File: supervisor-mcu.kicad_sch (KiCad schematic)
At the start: 20 parts, among them J21 ERF5-020-05.0-X-DV, J22 ERF5-020-05.0-X-DV

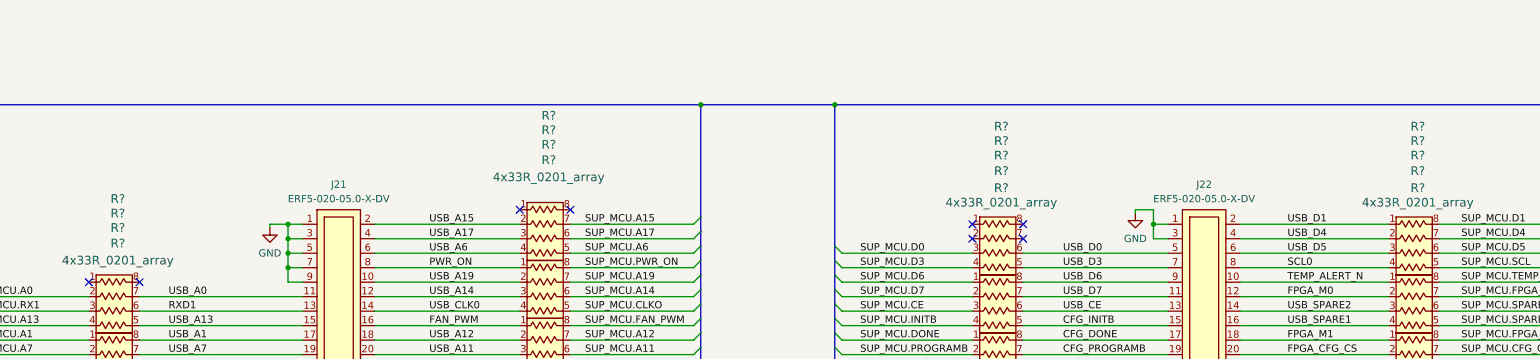
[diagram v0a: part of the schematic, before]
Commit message: Fix DDR3L placement
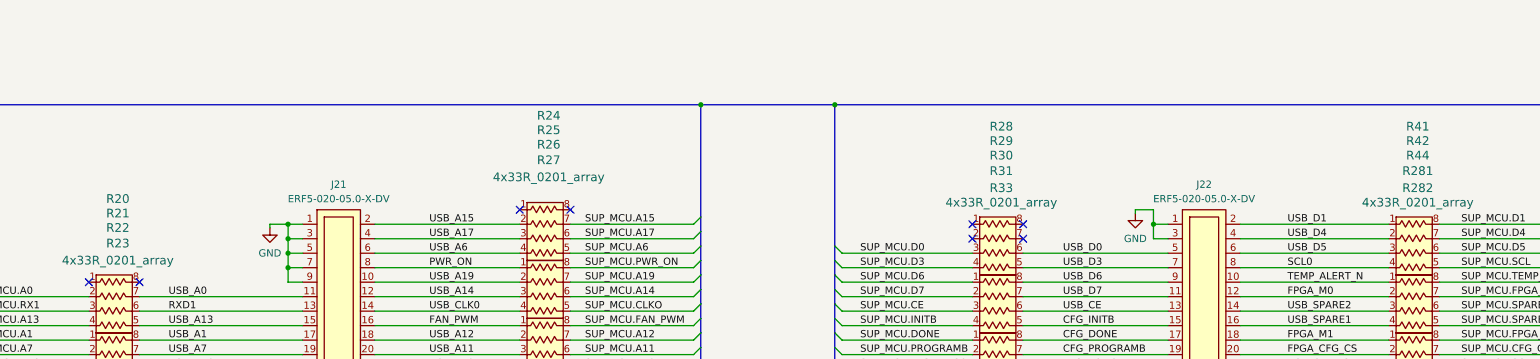
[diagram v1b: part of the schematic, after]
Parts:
- gave numbers to parts that had none: 18
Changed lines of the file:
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@@
   (symbol (lib_id "antmicroResistorNetworksArrays:4x33R_0201_array") (at 254 147.32 0) (unit 1)
     (in_bom yes) (on_board yes)
-    (property "Reference" "R?" (id 0) (at 254 104.775 0)
+    (property "Reference" "R30" (id 0) (at 254 104.775 0)
       (effects (font (size 1.524 1.524)))
     )
@@
   (symbol (lib_id "antmicroResistorNetworksArrays:4x33R_0201_array") (at 327.025 137.16 0) (unit 1)
     (in_bom yes) (on_board yes)
-    (property "Reference" "R?" (id 0) (at 327.025 102.235 0)
+    (property "Reference" "R42" (id 0) (at 327.025 102.235 0)
       (effects (font (size 1.524 1.524)))
     )
@@
   (symbol (lib_id "antmicroResistorNetworksArrays:4x33R_0201_array") (at 99.06 167.64 0) (unit 1)
     (in_bom yes) (on_board yes)
-    (property "Reference" "R?" (id 0) (at 99.06 120.1966 0)
+    (property "Reference" "R23" (id 0) (at 99.06 120.1966 0)
       (effects (font (size 1.524 1.524)))
     )
@@
   (symbol (lib_id "antmicroResistorNetworksArrays:4x33R_0201_array") (at 174.625 124.46 0) (unit 1)
     (in_bom yes) (on_board yes)
-    (property "Reference" "R?" (id 0) (at 174.625 97.79 0)
+    (property "Reference" "R24" (id 0) (at 174.625 97.79 0)
       (effects (font (size 1.524 1.524)))
     )
@@
   (symbol (lib_id "antmicroResistorNetworksArrays:4x33R_0201_array") (at 99.06 147.32 0) (unit 1)
     (in_bom yes) (on_board yes)
-    (property "Reference" "R?" (id 0) (at 99.06 114.935 0)
+    (property "Reference" "R21" (id 0) (at 99.06 114.935 0)
       (effects (font (size 1.524 1.524)))
     )
@@
   (symbol (lib_id "antmicroResistorNetworksArrays:4x33R_0201_array") (at 174.625 134.62 0) (unit 1)
     (in_bom yes) (on_board yes)
-    (property "Reference" "R?" (id 0) (at 174.625 100.33 0)
+    (property "Reference" "R25" (id 0) (at 174.625 100.33 0)
       (effects (font (size 1.524 1.524)))
     )
@@
   (symbol (lib_id "antmicroResistorNetworksArrays:4x33R_0201_array") (at 254 167.64 0) (unit 1)
     (in_bom yes) (on_board yes)
-    (property "Reference" "R?" (id 0) (at 254 110.49 0)
+    (property "Reference" "R33" (id 0) (at 254 110.49 0)
       (effects (font (size 1.524 1.524)))
     )
@@
   (symbol (lib_id "antmicroResistorNetworksArrays:4x33R_0201_array") (at 327.025 157.48 0) (unit 1)
     (in_bom yes) (on_board yes)
-    (property "Reference" "R?" (id 0) (at 327.025 107.4966 0)
+    (property "Reference" "R281" (id 0) (at 327.025 107.4966 0)
       (effects (font (size 1.524 1.524)))
     )
@@
   (symbol (lib_id "antmicroResistorNetworksArrays:4x33R_0201_array") (at 99.06 137.16 0) (unit 1)
     (in_bom yes) (on_board yes)
-    (property "Reference" "R?" (id 0) (at 99.06 112.395 0)
+    (property "Reference" "R20" (id 0) (at 99.06 112.395 0)
       (effects (font (size 1.524 1.524)))
     )
@@
   (symbol (lib_id "antmicroResistorNetworksArrays:4x33R_0201_array") (at 174.625 144.78 0) (unit 1)
     (in_bom yes) (on_board yes)
-    (property "Reference" "R?" (id 0) (at 174.625 102.87 0)
+    (property "Reference" "R26" (id 0) (at 174.625 102.87 0)
       (effects (font (size 1.524 1.524)))
     )
@@
   (symbol (lib_id "antmicroResistorNetworksArrays:4x33R_0201_array") (at 254 157.48 0) (unit 1)
     (in_bom yes) (on_board yes)
-    (property "Reference" "R?" (id 0) (at 254 107.4966 0)
+    (property "Reference" "R31" (id 0) (at 254 107.4966 0)
       (effects (font (size 1.524 1.524)))
     )
@@
   (symbol (lib_id "power:GND") (at 277.495 114.935 0) (unit 1)
     (in_bom yes) (on_board yes)
-    (property "Reference" "#PWR0450" (id 0) (at 279.4 64.135 0)
+    (property "Reference" "#PWR0457" (id 0) (at 279.4 64.135 0)
       (effects (font (size 1.27 1.27)) hide)
     )
@@
   (symbol (lib_id "power:+5V") (at 149.86 164.465 0) (mirror y) (unit 1)
     (in_bom yes) (on_board yes)
-    (property "Reference" "#PWR0448" (id 0) (at 149.86 168.275 0)
+    (property "Reference" "#PWR0456" (id 0) (at 149.86 168.275 0)
       (effects (font (size 1.27 1.27)) hide)
     )
@@
   (symbol (lib_id "antmicroResistorNetworksArrays:4x33R_0201_array") (at 327.025 167.64 0) (unit 1)
     (in_bom yes) (on_board yes)
-    (property "Reference" "R?" (id 0) (at 327.025 110.49 0)
+    (property "Reference" "R282" (id 0) (at 327.025 110.49 0)
       (effects (font (size 1.524 1.524)))
     )
@@
   (symbol (lib_id "antmicroResistorNetworksArrays:4x33R_0201_array") (at 174.625 154.94 0) (unit 1)
     (in_bom yes) (on_board yes)
-    (property "Reference" "R?" (id 0) (at 174.625 105.5916 0)
+    (property "Reference" "R27" (id 0) (at 174.625 105.5916 0)
       (effects (font (size 1.524 1.524)))
     )
@@
   (symbol (lib_id "antmicroResistorNetworksArrays:4x33R_0201_array") (at 327.025 127 0) (unit 1)
     (in_bom yes) (on_board yes)
-    (property "Reference" "R?" (id 0) (at 327.025 99.695 0)
+    (property "Reference" "R41" (id 0) (at 327.025 99.695 0)
       (effects (font (size 1.524 1.524)))
     )
@@
   (symbol (lib_id "antmicroResistorNetworksArrays:4x33R_0201_array") (at 254 127 0) (unit 1)
     (in_bom yes) (on_board yes)
-    (property "Reference" "R?" (id 0) (at 254 99.695 0)
+    (property "Reference" "R28" (id 0) (at 254 99.695 0)
       (effects (font (size 1.524 1.524)))
     )
@@
   (symbol (lib_id "antmicroResistorNetworksArrays:4x33R_0201_array") (at 327.025 147.32 0) (unit 1)
     (in_bom yes) (on_board yes)
-    (property "Reference" "R?" (id 0) (at 327.025 104.775 0)
+    (property "Reference" "R44" (id 0) (at 327.025 104.775 0)
       (effects (font (size 1.524 1.524)))
     )
@@
   (symbol (lib_id "antmicroResistorNetworksArrays:4x33R_0201_array") (at 254 137.16 0) (unit 1)
     (in_bom yes) (on_board yes)
-    (property "Reference" "R?" (id 0) (at 254 102.235 0)
+    (property "Reference" "R29" (id 0) (at 254 102.235 0)
       (effects (font (size 1.524 1.524)))
     )
@@
   (symbol (lib_id "antmicroResistorNetworksArrays:4x33R_0201_array") (at 99.06 157.48 0) (unit 1)
     (in_bom yes) (on_board yes)
-    (property "Reference" "R?" (id 0) (at 99.06 117.475 0)
-      (effects (font (size 1.524 1.524)))
-    )
+    (property "Reference" "R22" (id 0) (at 99.06 117.475 0)
+      (effects (font (size 1.524 1.524)))
+    )

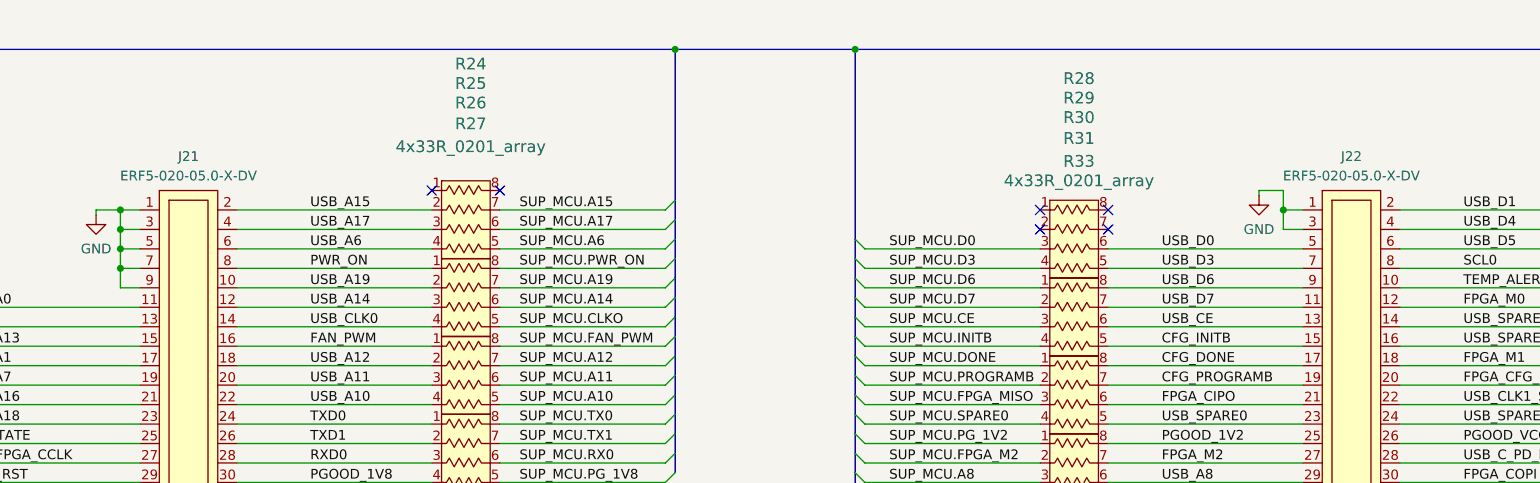
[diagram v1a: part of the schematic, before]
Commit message: Fix libraries, sync schematic with PCB
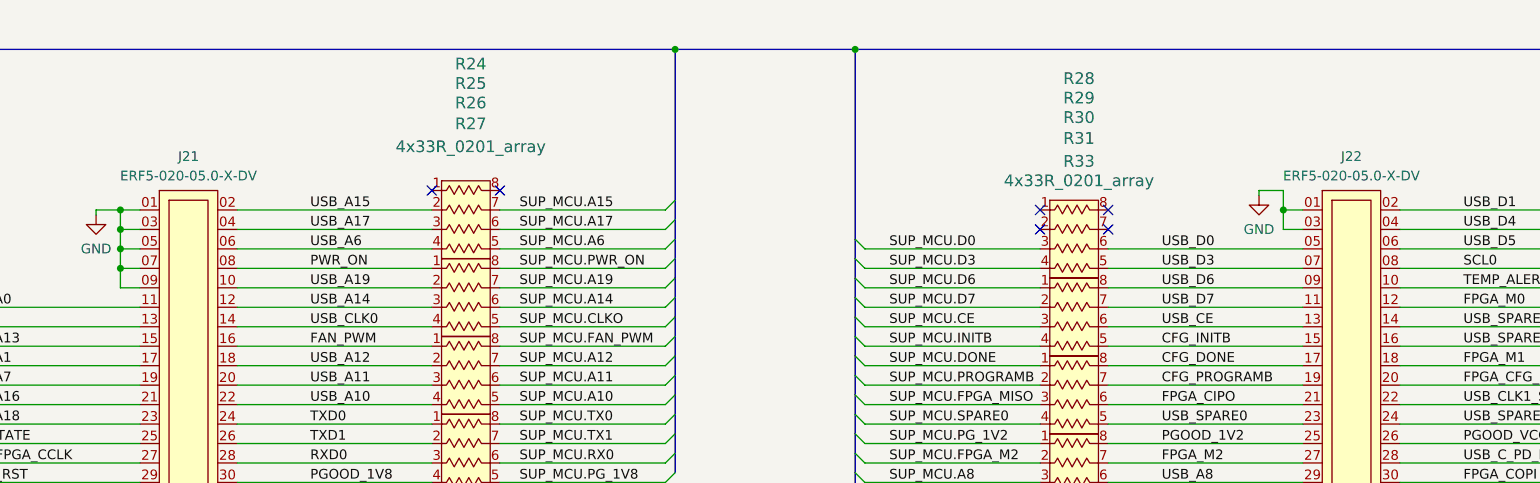
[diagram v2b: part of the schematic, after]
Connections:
- net GND: now also J21.01, J21.03, J21.05, J21.07, J21.09, J22.01, J22.03; no longer J21.1, J21.3, J21.5, J21.7, J21.9, J22.1, J22.3
- net PWR_ON: now also J21.08; no longer J21.8
- net SCL0: now also J22.08; no longer J22.8
- net USB_A15: now also J21.02; no longer J21.2
- net USB_A17: now also J21.04; no longer J21.4
- net USB_A6: now also J21.06; no longer J21.6
- net USB_D0: now also J22.05; no longer J22.5
- net USB_D1: now also J22.02; no longer J22.2
- net USB_D3: now also J22.07; no longer J22.7
- net USB_D4: now also J22.04; no longer J22.4
- net USB_D5: now also J22.06; no longer J22.6
- net USB_D6: now also J22.09; no longer J22.9
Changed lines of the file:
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@@
       (effects (font (size 1.27 1.27)) (justify left bottom) hide)
     )
-    (pin "1")
+    (pin "01")
+    (pin "02")
+    (pin "03")
+    (pin "04")
+    (pin "05")
+    (pin "06")
+    (pin "07")
+    (pin "08")
+    (pin "09")
     (pin "10")
     (pin "11")
@@
     (pin "18")
     (pin "19")
-    (pin "2")
     (pin "20")
     (pin "21")
@@
     (pin "28")
     (pin "29")
-    (pin "3")
     (pin "30")
     (pin "31")
@@
     (pin "38")
     (pin "39")
-    (pin "4")
     (pin "40")
-    (pin "5")
-    (pin "6")
-    (pin "7")
-    (pin "8")
-    (pin "9")
   )
   (symbol (lib_id "antmicroResistorNetworksArrays:4x33R_0201_array") (at 99.06 167.64 0) (unit 1)
@@
       (effects (font (size 1.27 1.27)) (justify left bottom) hide)
     )
-    (pin "1")
+    (pin "01")
+    (pin "02")
+    (pin "03")
+    (pin "04")
+    (pin "05")
+    (pin "06")
+    (pin "07")
+    (pin "08")
+    (pin "09")
     (pin "10")
     (pin "11")
@@
     (pin "18")
     (pin "19")
-    (pin "2")
     (pin "20")
     (pin "21")
@@
     (pin "28")
     (pin "29")
-    (pin "3")
     (pin "30")
     (pin "31")
@@
     (pin "38")
     (pin "39")
-    (pin "4")
     (pin "40")
-    (pin "5")
-    (pin "6")
-    (pin "7")
-    (pin "8")
-    (pin "9")
   )
   (symbol (lib_id "antmicroResistorNetworksArrays:4x33R_0201_array") (at 99.06 157.48 0) (unit 1)

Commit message: Finish connecting MCU
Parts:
- added NT? (x2): NetTie_2, antmicro-footprints:NetTie-2_SMD_Pad0.127mm, symbol antmicroShuntsJumpers:NetTie_2
- added R?: R_10k_0402, antmicro-footprints:0402-res, symbol antmicroResistors0402:R_10k_0402
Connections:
- net SUP_MCU.SDA: now also NT?.2, NT?.2
- net SUP_MCU.TEMP_ALERT_N: now also R?.1
- new net +3V3: R?.2
- new net I^{2}C.SCL: NT?.1
- new net I^{2}C.SDA: NT?.1

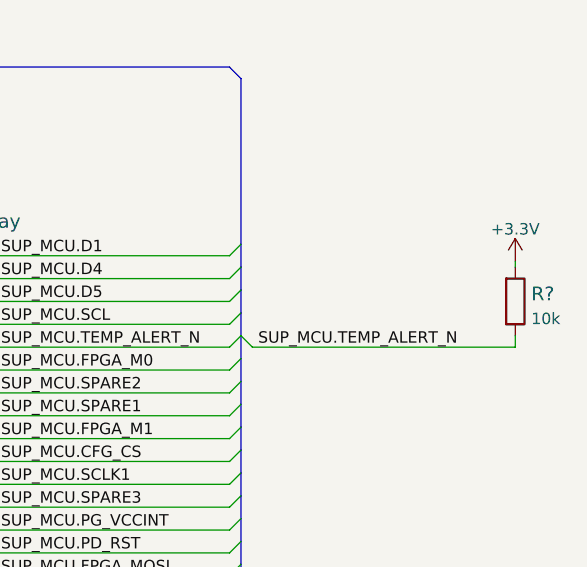
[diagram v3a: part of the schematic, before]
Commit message: Connect TEMP_ALERT_N signal to MCU
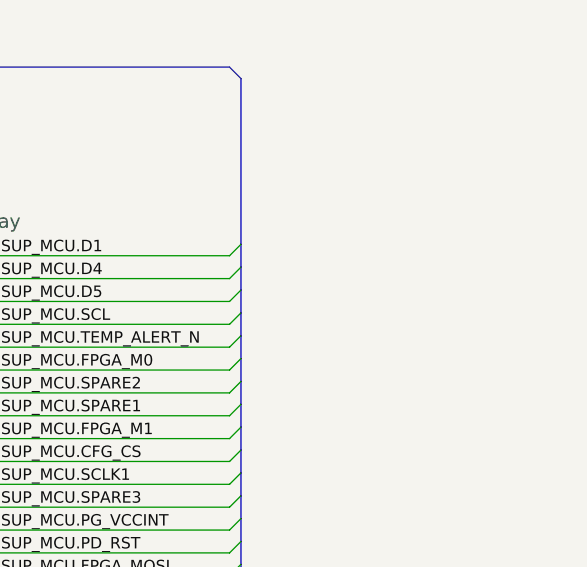
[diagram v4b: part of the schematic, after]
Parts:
- removed R?: R_10k_0402, antmicro-footprints:0402-res, symbol antmicroResistors0402:R_10k_0402
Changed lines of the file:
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@@
-    (stroke (width 0) (type default) (color 0 0 0 0))
-  )
-  (bus_entry (at 361.315 125.73) (size 1.27 1.27)
     (stroke (width 0) (type default) (color 0 0 0 0))
   )
@@
     (stroke (width 0) (type default) (color 0 0 0 0))
   )
-  (wire (pts (xy 391.795 117.475) (xy 391.795 118.11))
-    (stroke (width 0) (type default) (color 0 0 0 0))
-  )
   (wire (pts (xy 146.685 165.1) (xy 144.145 165.1))
     (stroke (width 0) (type default) (color 0 0 0 0))
@@
     (stroke (width 0) (type default) (color 0 0 0 0))
   )
-  (wire (pts (xy 362.585 127) (xy 391.795 127))
-    (stroke (width 0) (type default) (color 0 0 0 0))
-  )
   (wire (pts (xy 144.145 152.4) (xy 169.545 152.4))
     (stroke (width 0) (type default) (color 0 0 0 0))
@@
   )
   (wire (pts (xy 69.215 139.7) (xy 93.98 139.7))
-    (stroke (width 0) (type default) (color 0 0 0 0))
-  )
-  (wire (pts (xy 391.795 125.73) (xy 391.795 127))
     (stroke (width 0) (type default) (color 0 0 0 0))
   )
@@
   )
   (label "USB_D1" (at 304.165 116.84 0)
-    (effects (font (size 1.27 1.27)) (justify left bottom))
-  )
-  (label "SUP_MCU.TEMP_ALERT_N" (at 363.22 127 0)
     (effects (font (size 1.27 1.27)) (justify left bottom))
   )
@@
     )
     (pin "1")
-    (pin "2")
-  )
-  (symbol (lib_id "power:+3.3V") (at 391.795 117.475 0) (mirror y) (unit 1)
-    (in_bom yes) (on_board yes) (fields_autoplaced)
-    (property "Reference" "#PWR?" (id 0) (at 391.795 121.285 0)
-      (effects (font (size 1.27 1.27)) hide)
-    )
-    (property "Value" "+3.3V" (id 1) (at 391.795 113.8992 0))
-    (property "Footprint" "" (id 2) (at 391.795 117.475 0)
-      (effects (font (size 1.27 1.27)) hide)
-    )
-    (property "Datasheet" "" (id 3) (at 391.795 117.475 0)
-      (effects (font (size 1.27 1.27)) hide)
-    )
-    (pin "1")
-  )
-  (symbol (lib_id "antmicroResistors0402:R_10k_0402") (at 391.795 121.92 270) (mirror x) (unit 1)
-    (in_bom yes) (on_board yes) (fields_autoplaced)
-    (property "Reference" "R?" (id 0) (at 393.573 121.0854 90)
-      (effects (font (size 1.524 1.524)) (justify left))
-    )
-    (property "Value" "R_10k_0402" (id 1) (at 387.985 121.92 0)
-      (effects (font (size 1.524 1.524)) hide)
-    )
-    (property "Footprint" "antmicro-footprints:0402-res" (id 2) (at 396.875 116.84 0)
-      (effects (font (size 1.524 1.524)) (justify left) hide)
-    )
-    (property "Datasheet" "" (id 3) (at 391.795 121.92 0)
-      (effects (font (size 1.27 1.27)) hide)
-    )
-    (property "Manufacturer" "VISHAY" (id 4) (at 401.955 116.84 0)
-      (effects (font (size 1.524 1.524)) (justify left) hide)
-    )
-    (property "MPN" "CRCW040210K0FKEDHP" (id 5) (at 399.415 116.84 0)
-      (effects (font (size 1.524 1.524)) (justify left) hide)
-    )
-    (property "Val" "10k" (id 6) (at 393.573 123.8505 90)
-      (effects (font (size 1.27 1.27)) (justify left))
-    )
-    (pin "1")

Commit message: Fix libs, sync schematic with PCB
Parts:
- gave numbers to parts that had none: 2
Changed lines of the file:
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@@
   (symbol (lib_id "antmicroShuntsJumpers:NetTie_2") (at 45.085 101.6 0) (mirror x) (unit 1)
     (in_bom yes) (on_board yes) (fields_autoplaced)
-    (property "Reference" "NT?" (id 0) (at 45.085 102.87 0)
+    (property "Reference" "NT22" (id 0) (at 45.085 102.87 0)
       (effects (font (size 1.27 1.27)) hide)
     )
@@
   (symbol (lib_id "antmicroShuntsJumpers:NetTie_2") (at 45.085 104.14 0) (mirror x) (unit 1)
     (in_bom yes) (on_board yes) (fields_autoplaced)
-    (property "Reference" "NT?" (id 0) (at 45.085 105.41 0)
+    (property "Reference" "NT23" (id 0) (at 45.085 105.41 0)
       (effects (font (size 1.27 1.27)) hide)
     )

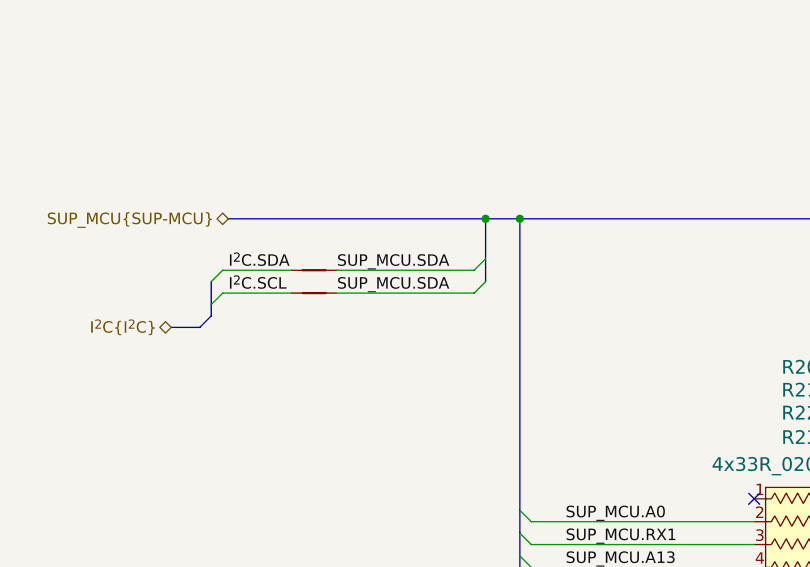
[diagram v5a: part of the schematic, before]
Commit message: Fix minor label missmatch. Continue placment
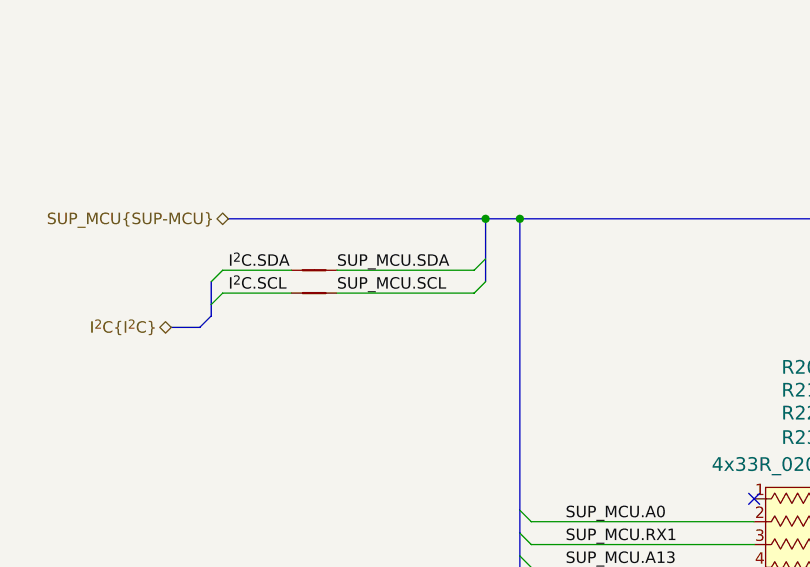
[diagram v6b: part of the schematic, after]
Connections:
- net SUP_MCU.SCL: now also NT23.2
- net SUP_MCU.SDA: no longer NT23.2
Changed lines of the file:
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@@
     (effects (font (size 1.27 1.27)) (justify left bottom))
   )
-  (label "SUP_MCU.SDA" (at 47.625 104.14 0)
+  (label "SUP_MCU.SCL" (at 47.625 104.14 0)
     (effects (font (size 1.27 1.27)) (justify left bottom))
   )

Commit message: Loclib
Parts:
- J21, J22: footprint antmicro-footprints:ERF5-020-05.0-X-DV -> K410T-devboard-footprints:ERF5-020-05.0-X-DV; symbol antmicroB2bConnectors:ERF5-020-05.0-X-DV -> K410T-devboard:ERF5-020-05.0-X-DV
- NT22, NT23: footprint antmicro-footprints:NetTie-2_SMD_Pad0.127mm -> K410T-devboard-footprints:NetTie-2_SMD_Pad0.127mm; symbol antmicroShuntsJumpers:NetTie_2 -> K410T-devboard:NetTie_2
- R20, R21, R22, R23, R24, R25, R26, R27, R28, R281, R282, R29, R30, R31, R33, R41, R42, R44: footprint antmicro-footprints:EXB18V -> K410T-devboard-footprints:EXB18V; symbol antmicroResistorNetworksArrays:4x33R_0201_array -> K410T-devboard:4x33R_0201_array
